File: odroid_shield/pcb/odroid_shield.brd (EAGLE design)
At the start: 83 x 48 mm, 71 parts, among them J1 AVRISP6_COMPACT, J4 ODROID_J4, U1 SINGLE-BIT_BUS_TRANSCEIVER, U10 ABM8G, U2 SINGLE-BIT_BUS_TRANSCEIVER, U3 ST1S10, U4 ATMEGA644P-20AU, U5 TS5205, U6 TCA9517MSOP8, U7 MP33926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

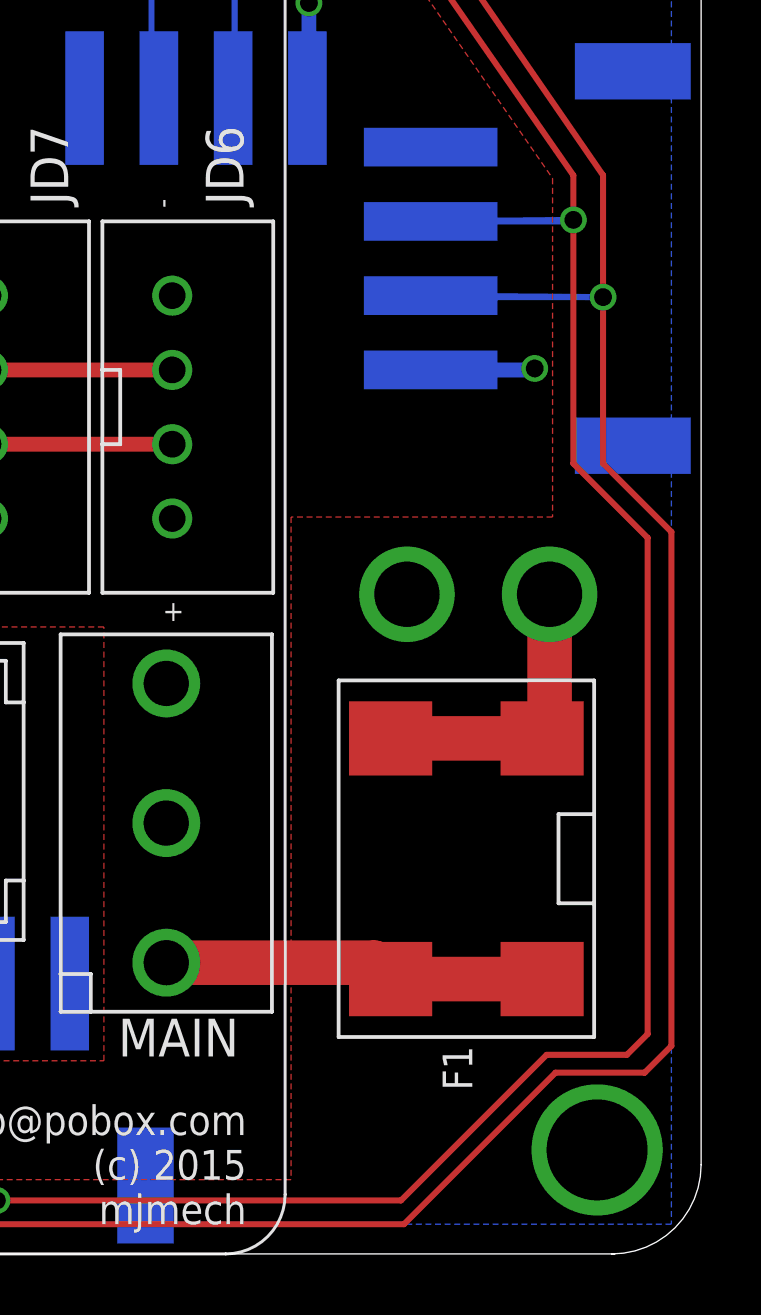
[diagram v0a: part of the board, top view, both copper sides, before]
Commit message: Update mammal chassis to a) leave another mm of room for connectors off the shield, and to leave a slot to make it easier to use both USB connectors.
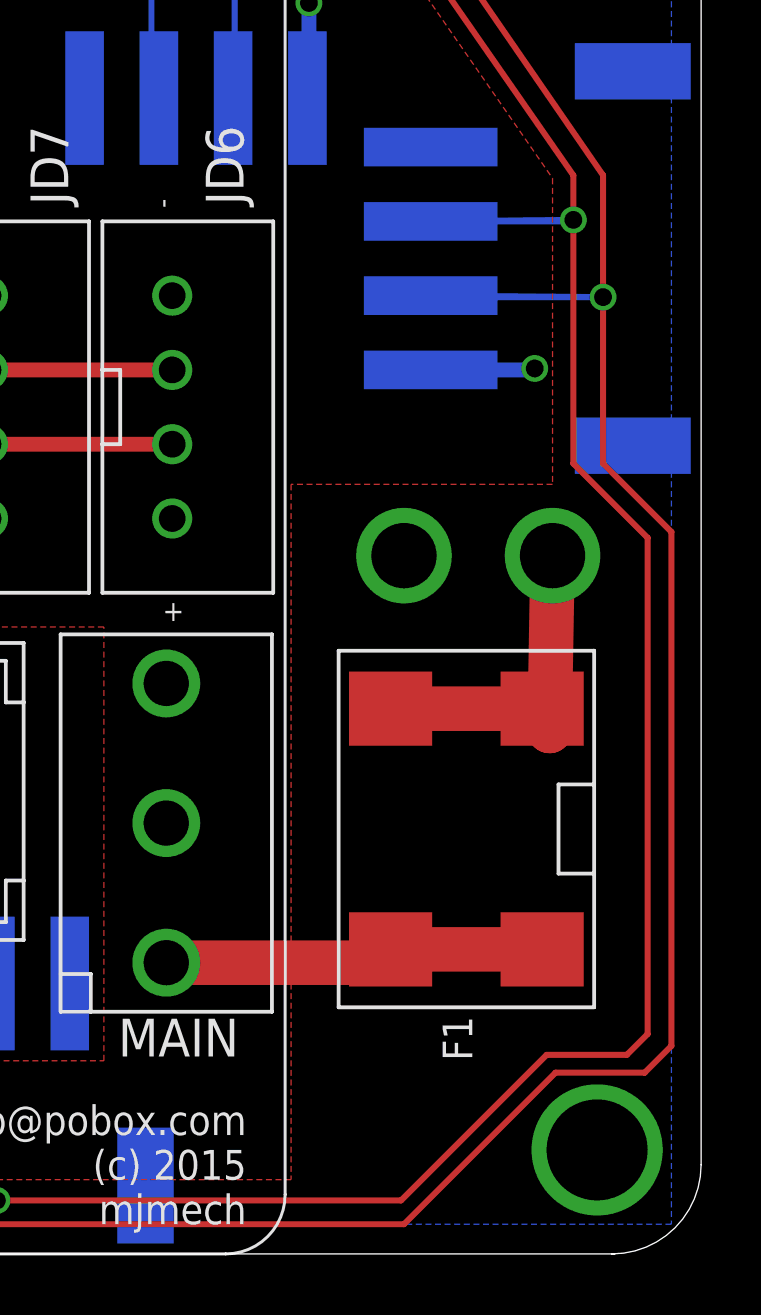
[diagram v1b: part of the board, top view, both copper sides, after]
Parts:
- moved B+ 1.30 mm to (78.0, 23.5)
- moved B- 1.30 mm to (73.0, 23.5)
- moved F1 1.00 mm to (75.1, 14.3)
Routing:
- net N$7: track 10.1 -> 11.8 mm
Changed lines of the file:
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@@
 <attribute name="NAME" x="67.6" y="35.3" size="1.27" layer="21" rot="R90"/>
 </element>
-<element name="B+" library="odroid_shield" package="BAT_TERM" value="BAT_TERM" x="77.9" y="22.2" smashed="yes" rot="MR0">
-<attribute name="NAME" x="81.26" y="23.34" size="1.27" layer="22" rot="MR270"/>
-</element>
-<element name="B-" library="odroid_shield" package="BAT_TERM" value="BAT_TERM" x="73.1" y="22.2" smashed="yes" rot="MR0">
-<attribute name="NAME" x="70.86" y="23.44" size="1.27" layer="22" rot="MR270"/>
+<element name="B+" library="odroid_shield" package="BAT_TERM" value="BAT_TERM" x="78" y="23.5" smashed="yes" rot="MR0">
+<attribute name="NAME" x="81.36" y="24.64" size="1.27" layer="22" rot="MR270"/>
+</element>
+<element name="B-" library="odroid_shield" package="BAT_TERM" value="BAT_TERM" x="73" y="23.5" smashed="yes" rot="MR0">
+<attribute name="NAME" x="70.76" y="24.74" size="1.27" layer="22" rot="MR270"/>
 </element>
 <element name="ARM" library="led" package="LED5MM" value="FLASH_RED" x="22.6" y="36" smashed="yes" rot="R90">
@@
 <attribute name="VALUE" x="21.375" y="2.72" size="1.27" layer="27" rot="R90"/>
 </element>
-<element name="F1" library="odroid_shield" package="KEYSTONE_HORIZ_FUSE_CLIP" value="FUSE" x="75.1" y="13.3" smashed="yes" rot="R90">
-<attribute name="DPN" value="36-3569-ND" x="75.1" y="13.3" size="1.778" layer="27" rot="R90" display="off"/>
-<attribute name="NAME" x="74.3" y="7" size="1" layer="21" ratio="10" rot="R270"/>
+<element name="F1" library="odroid_shield" package="KEYSTONE_HORIZ_FUSE_CLIP" value="FUSE" x="75.1" y="14.3" smashed="yes" rot="R90">
+<attribute name="DPN" value="36-3569-ND" x="75.1" y="14.3" size="1.778" layer="27" rot="R90" display="off"/>
+<attribute name="NAME" x="74.3" y="8" size="1" layer="21" ratio="10" rot="R270"/>
 </element>
 <element name="U3" library="odroid_shield" package="POWER_SO8" value="ST1S10" x="42.2" y="13.6" smashed="yes" rot="R270">
@@
 <contactref element="F1" pad="2"/>
 <wire x1="65" y1="9.801" x2="71.999" y2="9.801" width="1.5" layer="1"/>
-<wire x1="71.999" y1="9.801" x2="72.55" y2="9.25" width="1.5" layer="1"/>
-<wire x1="72.55" y1="9.25" x2="77.65" y2="9.25" width="1.5" layer="1"/>
+<wire x1="71.999" y1="9.801" x2="72.55" y2="10.25" width="1.5" layer="1"/>
+<wire x1="72.55" y1="10.25" x2="77.65" y2="10.25" width="1.5" layer="1"/>
 </signal>
 <signal name="N$7">
@@
 <contactref element="F1" pad="3"/>
 <contactref element="F1" pad="4"/>
-<wire x1="77.9" y1="22.2" x2="77.9" y2="17.6" width="1.5" layer="1"/>
-<wire x1="77.9" y1="17.6" x2="77.65" y2="17.35" width="1.5" layer="1"/>
-<wire x1="77.65" y1="17.35" x2="72.55" y2="17.35" width="1.5" layer="1"/>
+<wire x1="78" y1="23.5" x2="77.9" y2="17.6" width="1.5" layer="1"/>
+<wire x1="77.9" y1="17.6" x2="77.65" y2="18.35" width="1.5" layer="1"/>
+<wire x1="77.65" y1="18.35" x2="72.55" y2="18.35" width="1.5" layer="1"/>
 </signal>
 <signal name="N$11">
@@
 <vertex x="72.1" y="44.7"/>
 <vertex x="78" y="36.2"/>
-<vertex x="78" y="24.8"/>
-<vertex x="69.2" y="24.8"/>
+<vertex x="78" y="25.9"/>
+<vertex x="69.2" y="25.9"/>
 <vertex x="69.2" y="2.5"/>
 <vertex x="33.9" y="2.5"/>

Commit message: Correctly name the motor driver (the correct datasheet was checked in).
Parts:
- U7: value MP33926 -> MC33926
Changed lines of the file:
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@@
 <attribute name="NAME" x="54.035" y="8.065" size="1" layer="25" ratio="10" rot="R180"/>
 </element>
-<element name="U7" library="odroid_shield" package="PQFN32" value="MP33926" x="41.2" y="33.1" smashed="yes">
+<element name="U7" library="odroid_shield" package="PQFN32" value="MC33926" x="41.2" y="33.1" smashed="yes">
 <attribute name="NAME" x="44.6" y="37.8" size="1" layer="21" ratio="10"/>
+<attribute name="DPN" value="MC33926PNB-ND" x="41.2" y="33.1" size="1.778" layer="27" display="off"/>
 </element>
 <element name="C6" library="rcl" package="C0603" value=".1uF" x="37.1" y="38.8" smashed="yes" rot="R180">

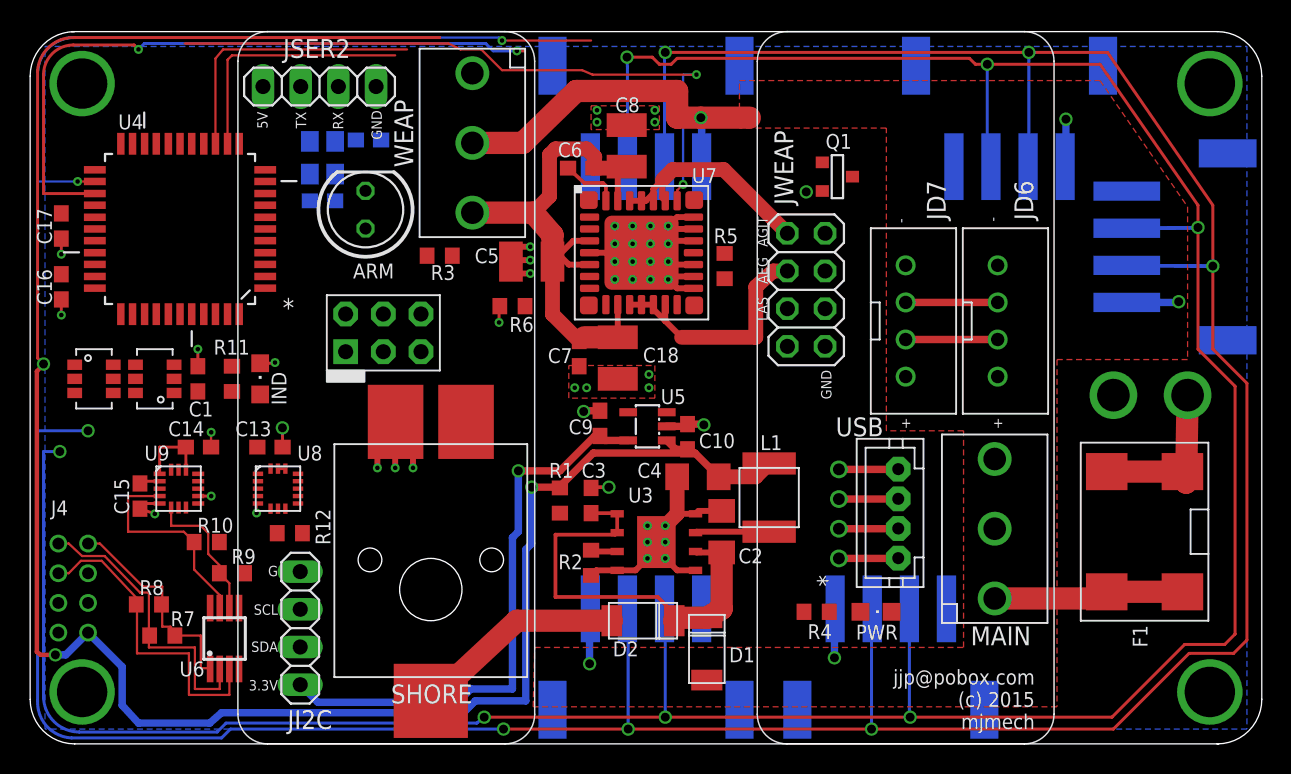
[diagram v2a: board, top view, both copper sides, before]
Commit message: odroid_shield: Fully routed version with silks moved off vias.
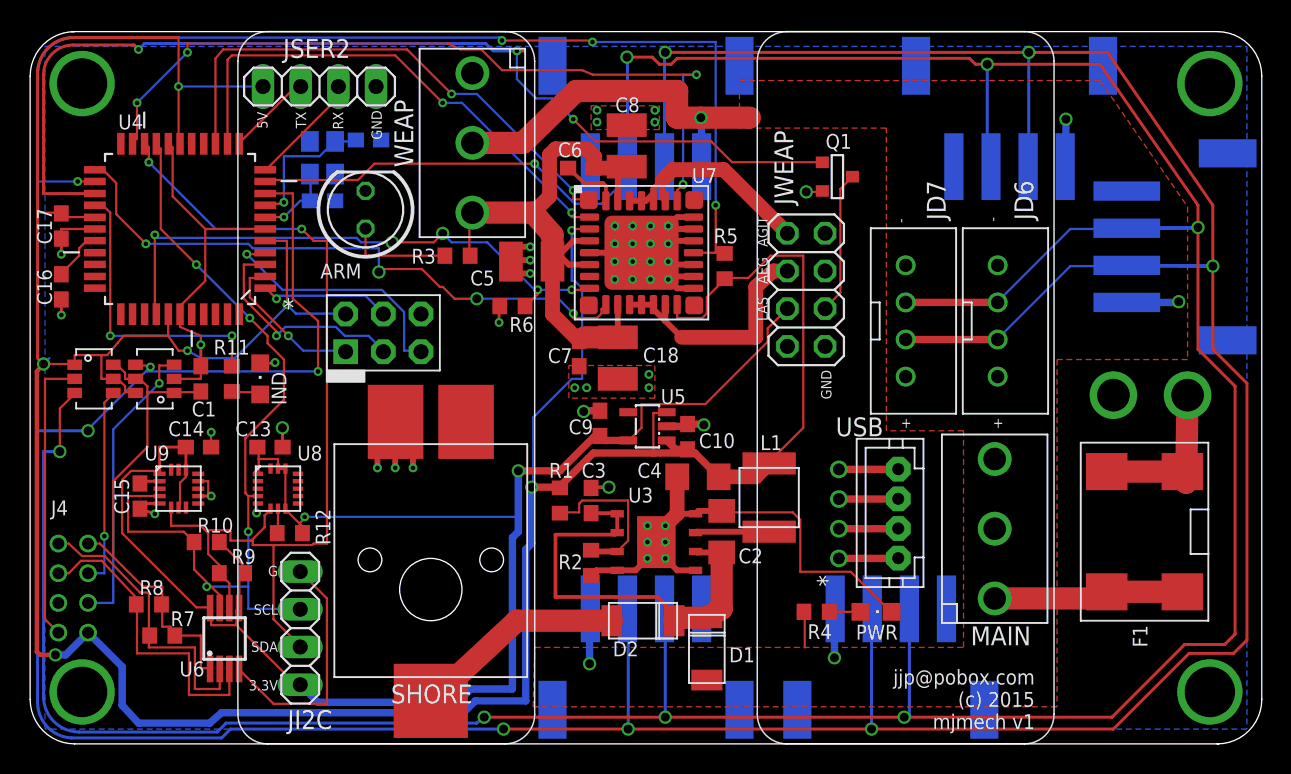
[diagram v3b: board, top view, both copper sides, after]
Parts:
- moved R3 1.20 mm to (28.8, 32.9)
- moved C1 0.20 mm to (11.5, 24.6)
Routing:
- net +5V: track 140.0 -> 227.4 mm, vias 3 -> 7
- net GND: track 55.4 -> 138.3 mm
- net +3V3: track 44.1 -> 116.4 mm, vias 1 -> 2
- net SYS_SDA: track 9.57 -> 65.0 mm, vias 0 -> 2
- net ODROID_TX_5V: track 229.0 -> 273.2 mm, vias 7 -> 9
- net SYS_SCL: track 14.4 -> 57.7 mm, vias 0 -> 4
- net ODROID_RX_5V: track 220.6 -> 263.6 mm, vias 7 -> 8
- net MOTOR_EN: track 0.00 -> 41.7 mm, vias 0 -> 4
- net MOTOR_FB: track 0.00 -> 38.3 mm, vias 0 -> 5
- net LASER_EN: track 45.2 -> 70.0 mm, vias 2 -> 3
- net MOTOR_SF: track 49.5 -> 74.3 mm, vias 2 -> 4
- net N$4: track 0.00 -> 20.0 mm, vias 0 -> 1
- net N$17: track 0.00 -> 19.8 mm, vias 0 -> 2
- net VCCIO: track 14.8 -> 34.1 mm
- net AEG_PWM: track 17.1 -> 34.9 mm, vias 0 -> 2
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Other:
- board text added: "mjmech v1"
- board text removed: "mjmech"
